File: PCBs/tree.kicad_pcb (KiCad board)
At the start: 2 copper layers, 31 parts, among them J1 Conn_01x06_Female, SW1 SW_Push_DPDT, SW2 SW_SPST, U1 Shift_Reg, U2 Shift_Reg, U3 Shift_Reg, U4 pic18f45k20

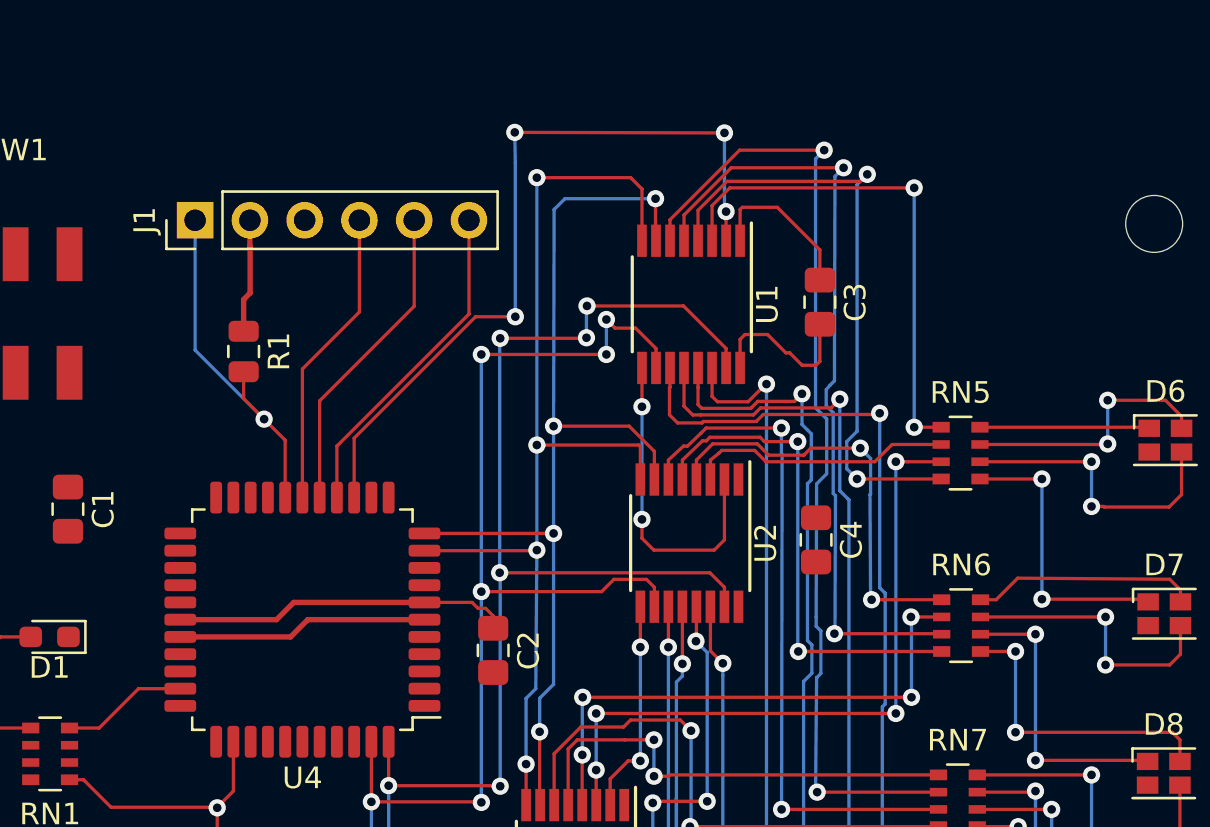
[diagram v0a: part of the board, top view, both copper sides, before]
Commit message: Added J2 for a debug/Logic probe header
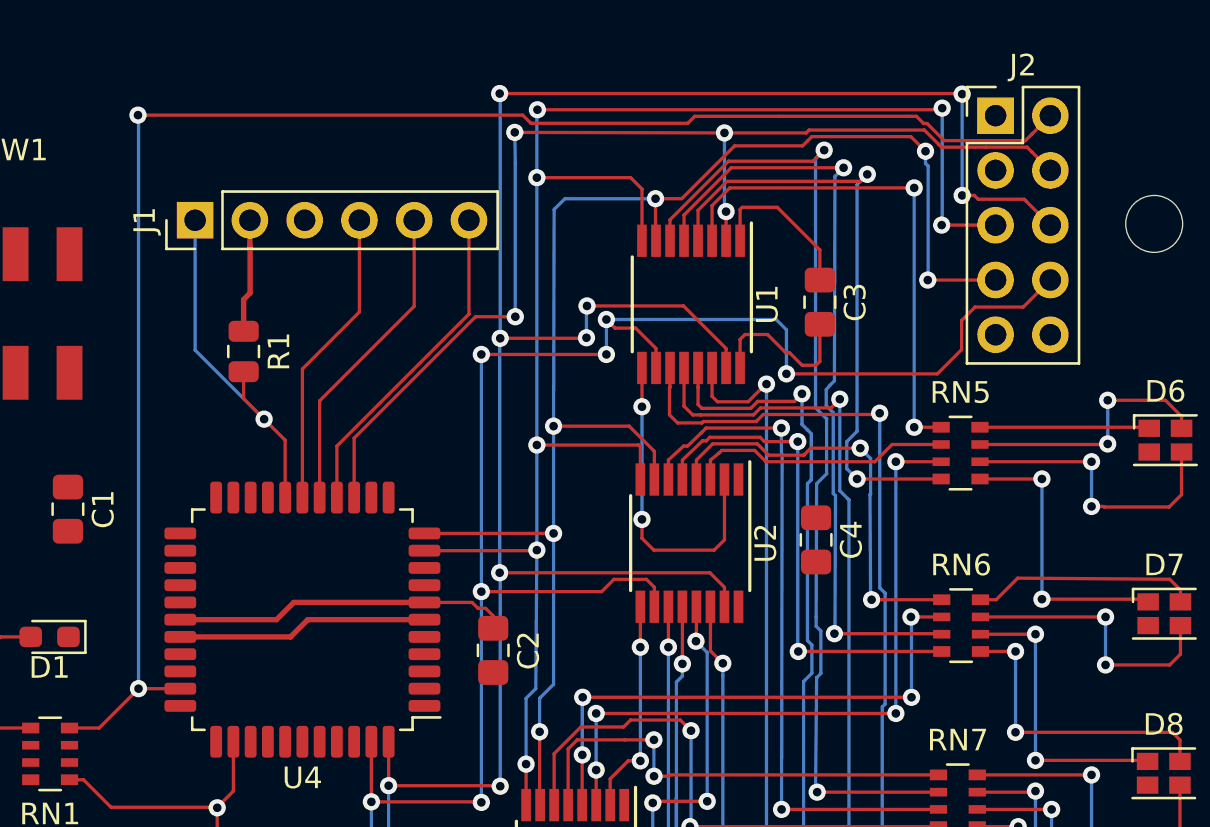
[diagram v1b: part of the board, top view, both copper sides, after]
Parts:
- added J2: Conn_02x05_Odd_Even, Connector_PinHeader_2.54mm:PinHeader_2x05_P2.54mm_Vertical, F.Cu at (211.5, 72.1)
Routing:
- net HB: track 5.89 -> 76.1 mm, vias 0 -> 2
- net Shift_CLK: track 70.2 -> 112.4 mm, vias 7 -> 10
- net ~Output_Enable~: track 48.4 -> 78.3 mm, vias 4 -> 7
- net Storage_CLK: track 63.1 -> 88.5 mm, vias 7 -> 8
- net ~MEM_RESET~: track 47.2 -> 70.4 mm, vias 4 -> 6
- net Red_Data: track 35.9 -> 51.9 mm

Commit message: finished layout and generated gerbers
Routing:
- net Net-(BT1-Pad2): track 0.00 -> 66.8 mm
- net GND: track 19.2 -> 44.7 mm, vias 0 -> 7
- net 3v3: track 28.4 -> 46.6 mm
- net Net-(BT1-Pad1): track 0.00 -> 10.1 mm
- net Green_Data: track 14.9 -> 12.4 mm
- added copper zone on F.Cu, net 3v3
- added copper zone on B.Cu, net GND
- removed copper zone on F.Cu, net BT1
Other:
- board outline added: 83.8 x 59.9 mm
- board text added: "1"
- board text added: "HB"
- board text added: "Off"
- board text added: "On"
